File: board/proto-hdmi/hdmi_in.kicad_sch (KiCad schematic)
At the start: 44 parts, among them J2 HDMI_A, SW1 CTS_218-4LPSTR, U1 NTS0302, U3 M24C02, U4 74LVC1G17

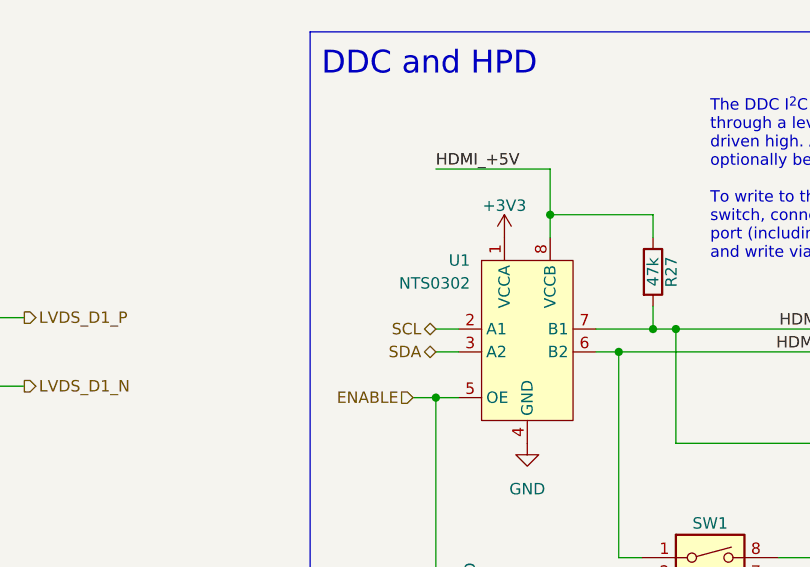
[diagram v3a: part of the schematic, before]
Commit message: Export boards for manufacturing.
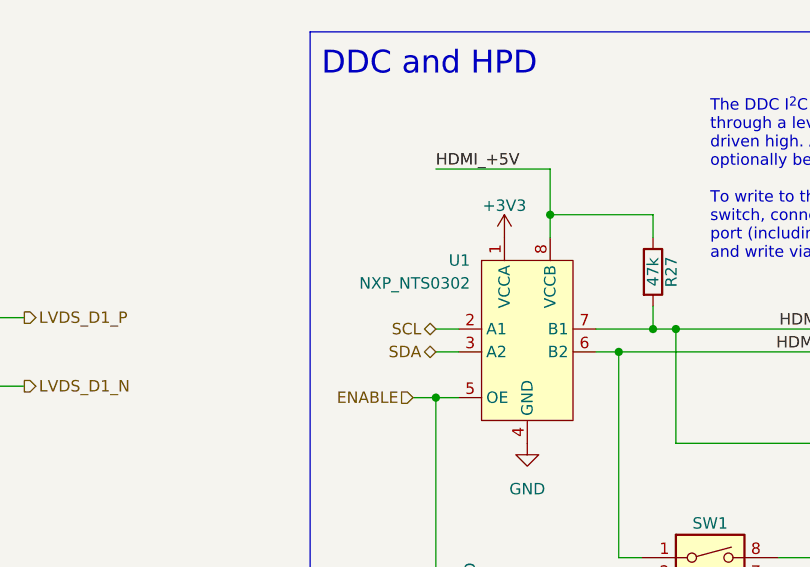
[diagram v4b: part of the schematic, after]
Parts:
- U1: value NTS0302 -> NXP_NTS0302
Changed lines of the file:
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@@
       (effects (font (size 1.27 1.27)) (justify right))
     )
-    (property "Value" "NTS0302" (id 1) (at 195.58 104.14 0)
+    (property "Value" "NXP_NTS0302" (id 1) (at 195.58 104.14 0)
       (effects (font (size 1.27 1.27)) (justify right))
     )

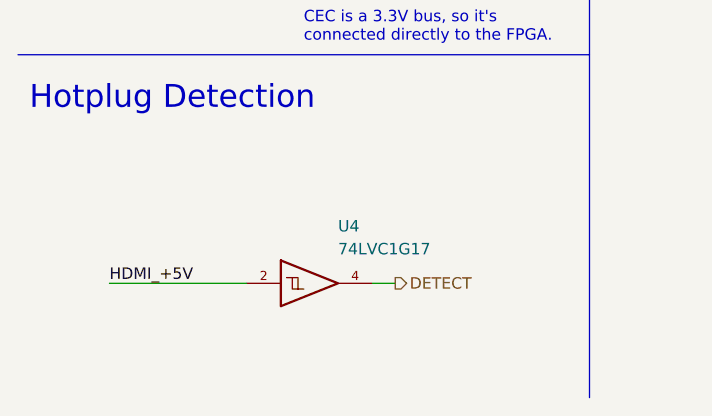
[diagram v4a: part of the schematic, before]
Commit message: Fix 1G17QDRY pinout.
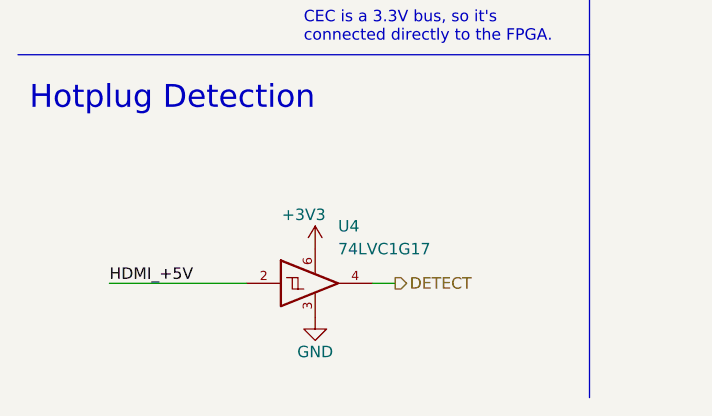
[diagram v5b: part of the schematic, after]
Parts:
- U4: symbol 74xGxx:74LVC1G17 -> 0Local:74LVC1G17QDRY
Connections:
- net +3V3: now also U4.6
- net VCC: no longer names the net of U4.5
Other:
- company: © 2022 Sam Hanes, licensed under CERN-OHL-P v2 -> © 2022 Sam Hanes, licensed under CERN-OHL-S v2
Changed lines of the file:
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@@
   (title_block
     (title "HDMI Expansion for Olimex ICE40HX8K-EVB")
-    (date "2022-04-19")
-    (rev "0.1")
-    (company "© 2022 Sam Hanes, licensed under CERN-OHL-P v2")
+    (date "2022-08-04")
+    (rev "0.2")
+    (company "© 2022 Sam Hanes, licensed under CERN-OHL-S v2")
     (comment 1 "https://github.com/Elemecca/1240pi")
   )
@@
     (pin "2")
   )
-  (symbol (lib_id "74xGxx:74LVC1G17") (at 45.72 190.5 0) (unit 1)
+  (symbol (lib_id "0Local:74LVC1G17QDRY") (at 45.72 190.5 0) (unit 1)
     (in_bom yes) (on_board yes)
     (property "Reference" "U4" (id 0) (at 48.26 184.15 0)
@@
       (effects (font (size 1.27 1.27)) (justify left))
     )
-    (property "Footprint" "Package_TO_SOT_SMD:SOT-886" (id 2) (at 45.72 190.5 0)
-      (effects (font (size 1.27 1.27)) hide)
-    )
-    (property "Datasheet" "http://www.ti.com/lit/sg/scyt129e/scyt129e.pdf" (id 3) (at 45.72 190.5 0)
-      (effects (font (size 1.27 1.27)) hide)
-    )
+    (property "Footprint" "Package_TO_SOT_SMD:SOT-886" (id 2) (at 45.72 199.39 0)
+      (effects (font (size 1.27 1.27)) hide)
+    )
+    (property "Datasheet" "https://www.ti.com/lit/ds/symlink/sn74lvc1g17-q1.pdf" (id 3) (at 45.72 201.93 0)
+      (effects (font (size 1.27 1.27)) hide)
+    )
+    (pin "1")
     (pin "2")
     (pin "3")
     (pin "4")
     (pin "5")
+    (pin "6")
   )
   (symbol (lib_id "Device:C") (at 123.19 115.57 90) (unit 1)
@@
     (pin "1")
     (pin "2")
+  )
+  (symbol (lib_id "power:GND") (at 45.72 194.31 0) (unit 1)
+    (in_bom yes) (on_board yes)
+    (property "Reference" "#PWR0128" (id 0) (at 45.72 200.66 0)
+      (effects (font (size 1.27 1.27)) hide)
+    )
+    (property "Value" "GND" (id 1) (at 45.72 198.12 0))
+    (property "Footprint" "" (id 2) (at 45.72 194.31 0)
+      (effects (font (size 1.27 1.27)) hide)
+    )
+    (property "Datasheet" "" (id 3) (at 45.72 194.31 0)
+      (effects (font (size 1.27 1.27)) hide)
+    )
+    (pin "1")
   )
   (symbol (lib_id "Device:R") (at 139.7 101.6 180) (unit 1)
@@
     (pin "2")
   )
+  (symbol (lib_id "power:+3V3") (at 45.72 186.69 0) (unit 1)
+    (in_bom yes) (on_board yes)
+    (property "Reference" "#PWR0129" (id 0) (at 45.72 190.5 0)
+      (effects (font (size 1.27 1.27)) hide)
+    )
+    (property "Value" "+3V3" (id 1) (at 44.45 182.88 0))
+    (property "Footprint" "" (id 2) (at 45.72 186.69 0)
+      (effects (font (size 1.27 1.27)) hide)
+    )
+    (property "Datasheet" "" (id 3) (at 45.72 186.69 0)
+      (effects (font (size 1.27 1.27)) hide)
+    )
+    (pin "1")
+  )
   (symbol (lib_id "Device:C") (at 205.74 39.37 90) (unit 1)
